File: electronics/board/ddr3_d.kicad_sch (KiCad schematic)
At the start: 22 parts, among them U4 DDR3-78

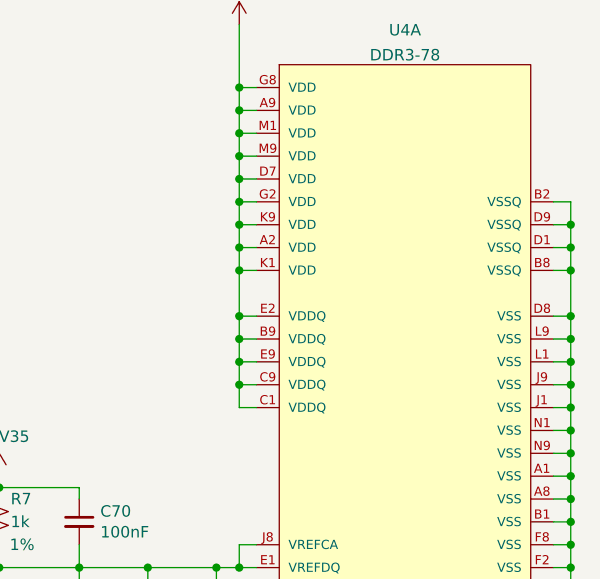
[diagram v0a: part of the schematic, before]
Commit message: Added gitignore, fixed the part
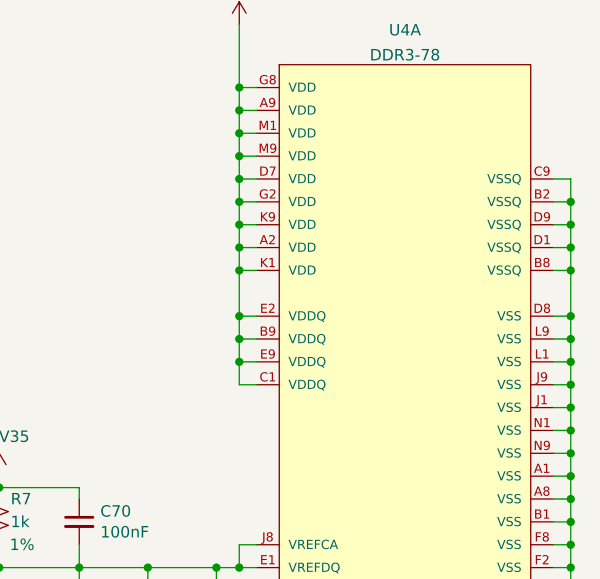
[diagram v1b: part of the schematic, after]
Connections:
- net +1V35: no longer U4.C9 (VDDQ)
- net GND: now also U4.C9 (VSSQ)
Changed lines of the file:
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@@
   (junction (at 222.25 105.41) (diameter 0) (color 0 0 0 0)
   )
-  (junction (at 185.42 102.87) (diameter 0) (color 0 0 0 0)
-  )
   (junction (at 222.25 100.33) (diameter 0) (color 0 0 0 0)
   )
@@
   (junction (at 222.25 110.49) (diameter 0) (color 0 0 0 0)
   )
+  (junction (at 222.25 82.55) (diameter 0) (color 0 0 0 0)
+  )
   (junction (at 222.25 115.57) (diameter 0) (color 0 0 0 0)
   )
@@
     (stroke (width 0) (type default) (color 0 0 0 0))
   )
+  (wire (pts (xy 220.345 80.01) (xy 222.25 80.01))
+    (stroke (width 0) (type default) (color 0 0 0 0))
+  )
   (wire (pts (xy 185.42 69.85) (xy 185.42 72.39))
     (stroke (width 0) (type default) (color 0 0 0 0))
@@
     (stroke (width 0) (type default) (color 0 0 0 0))
   )
-  (wire (pts (xy 185.42 102.87) (xy 185.42 105.41))
-    (stroke (width 0) (type default) (color 0 0 0 0))
-  )
   (bus (pts (xy 57.15 72.39) (xy 57.15 74.93))
     (stroke (width 0) (type default) (color 0 0 0 0))
   )
-  (wire (pts (xy 187.325 105.41) (xy 185.42 105.41))
-    (stroke (width 0) (type default) (color 0 0 0 0))
-  )
   (wire (pts (xy 146.685 64.135) (xy 146.685 57.785))
     (stroke (width 0) (type default) (color 0 0 0 0))
@@
     (stroke (width 0) (type default) (color 0 0 0 0))
   )
+  (wire (pts (xy 222.25 80.01) (xy 222.25 82.55))
+    (stroke (width 0) (type default) (color 0 0 0 0))
+  )
